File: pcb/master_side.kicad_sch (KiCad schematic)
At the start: 85 parts, among them IC1 PCA9956BTWY, J1 USB_C_Receptacle_USB2.0_14P, J2 Conn_01x02, J5 4P4C, SW1 SW_SP3T, SW10 SW_Push_45deg, SW11 SW_Push_45deg, SW12 SW_Push_45deg, SW13 SW_Push_45deg, SW14 SW_Push_45deg, SW15 SW_Push_45deg, SW16 SW_Push_45deg, SW17 SW_Push_45deg, SW18 SW_Push_45deg, SW19 SW_Push_45deg, SW2 SW_Push_45deg, SW3 SW_Push_45deg, SW4 SW_Push_45deg, SW5 SW_Push_45deg, SW6 SW_Push_45deg, SW7 SW_Push_45deg, SW8 SW_Push_45deg, SW9 SW_Push_45deg, U1 W25Q128JVSIQ, U2 RP2040, U3 NCP1117LPST33T3G, U4 OPT3001DNPR, Y1 ABM8-272-T3

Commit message: fix: revert to proper switch footprint without SMD LED
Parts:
- SW10, SW11, SW12, SW13, SW14, SW15, SW16, SW17, SW18, SW19, SW2, SW3, SW4, SW5, SW6, SW7, SW8, SW9: footprint ai03-MX_V2:MX-LED -> ai03-MX_V2:MX-Solderable-1U
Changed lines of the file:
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@@
 			)
 		)
-		(property "Footprint" "ai03-MX_V2:MX-LED"
+		(property "Footprint" "ai03-MX_V2:MX-Solderable-1U"
 			(at 384.81 298.45 0)
 			(effects
@@
 			)
 		)
-		(property "Footprint" "ai03-MX_V2:MX-LED"
+		(property "Footprint" "ai03-MX_V2:MX-Solderable-1U"
 			(at 407.67 298.45 0)
 			(effects
@@
 			)
 		)
-		(property "Footprint" "ai03-MX_V2:MX-LED"
+		(property "Footprint" "ai03-MX_V2:MX-Solderable-1U"
 			(at 396.24 326.39 0)
 			(effects
@@
 			)
 		)
-		(property "Footprint" "ai03-MX_V2:MX-LED"
+		(property "Footprint" "ai03-MX_V2:MX-Solderable-1U"
 			(at 430.53 298.45 0)
 			(effects
@@
 			)
 		)
-		(property "Footprint" "ai03-MX_V2:MX-LED"
+		(property "Footprint" "ai03-MX_V2:MX-Solderable-1U"
 			(at 384.81 326.39 0)
 			(effects
@@
 			)
 		)
-		(property "Footprint" "ai03-MX_V2:MX-LED"
+		(property "Footprint" "ai03-MX_V2:MX-Solderable-1U"
 			(at 384.81 312.42 0)
 			(effects
@@
 			)
 		)
-		(property "Footprint" "ai03-MX_V2:MX-LED"
+		(property "Footprint" "ai03-MX_V2:MX-Solderable-1U"
 			(at 407.67 312.42 0)
 			(effects
@@
 			)
 		)
-		(property "Footprint" "ai03-MX_V2:MX-LED"
+		(property "Footprint" "ai03-MX_V2:MX-Solderable-1U"
 			(at 419.1 312.42 0)
 			(effects
@@
 			)
 		)
-		(property "Footprint" "ai03-MX_V2:MX-LED"
+		(property "Footprint" "ai03-MX_V2:MX-Solderable-1U"
 			(at 373.38 312.42 0)
 			(effects
@@
 			)
 		)
-		(property "Footprint" "ai03-MX_V2:MX-LED"
+		(property "Footprint" "ai03-MX_V2:MX-Solderable-1U"
 			(at 373.38 298.45 0)
 			(effects
@@
 			)
 		)
-		(property "Footprint" "ai03-MX_V2:MX-LED"
+		(property "Footprint" "ai03-MX_V2:MX-Solderable-1U"
 			(at 430.53 326.39 0)
 			(effects
@@
 			)
 		)
-		(property "Footprint" "ai03-MX_V2:MX-LED"
+		(property "Footprint" "ai03-MX_V2:MX-Solderable-1U"
 			(at 373.38 326.39 0)
 			(effects
@@
 			)
 		)
-		(property "Footprint" "ai03-MX_V2:MX-LED"
+		(property "Footprint" "ai03-MX_V2:MX-Solderable-1U"
 			(at 430.53 312.42 0)
 			(effects
@@
 			)
 		)
-		(property "Footprint" "ai03-MX_V2:MX-LED"
+		(property "Footprint" "ai03-MX_V2:MX-Solderable-1U"
 			(at 396.24 312.42 0)
 			(effects
@@
 			)
 		)
-		(property "Footprint" "ai03-MX_V2:MX-LED"
+		(property "Footprint" "ai03-MX_V2:MX-Solderable-1U"
 			(at 407.67 326.39 0)
 			(effects
@@
 			)
 		)
-		(property "Footprint" "ai03-MX_V2:MX-LED"
+		(property "Footprint" "ai03-MX_V2:MX-Solderable-1U"
 			(at 419.1 298.45 0)
 			(effects
@@
 			)
 		)
-		(property "Footprint" "ai03-MX_V2:MX-LED"
+		(property "Footprint" "ai03-MX_V2:MX-Solderable-1U"
 			(at 396.24 298.45 0)
 			(effects
@@
 			)
 		)
-		(property "Footprint" "ai03-MX_V2:MX-LED"
+		(property "Footprint" "ai03-MX_V2:MX-Solderable-1U"
 			(at 419.1 326.39 0)
 			(effects

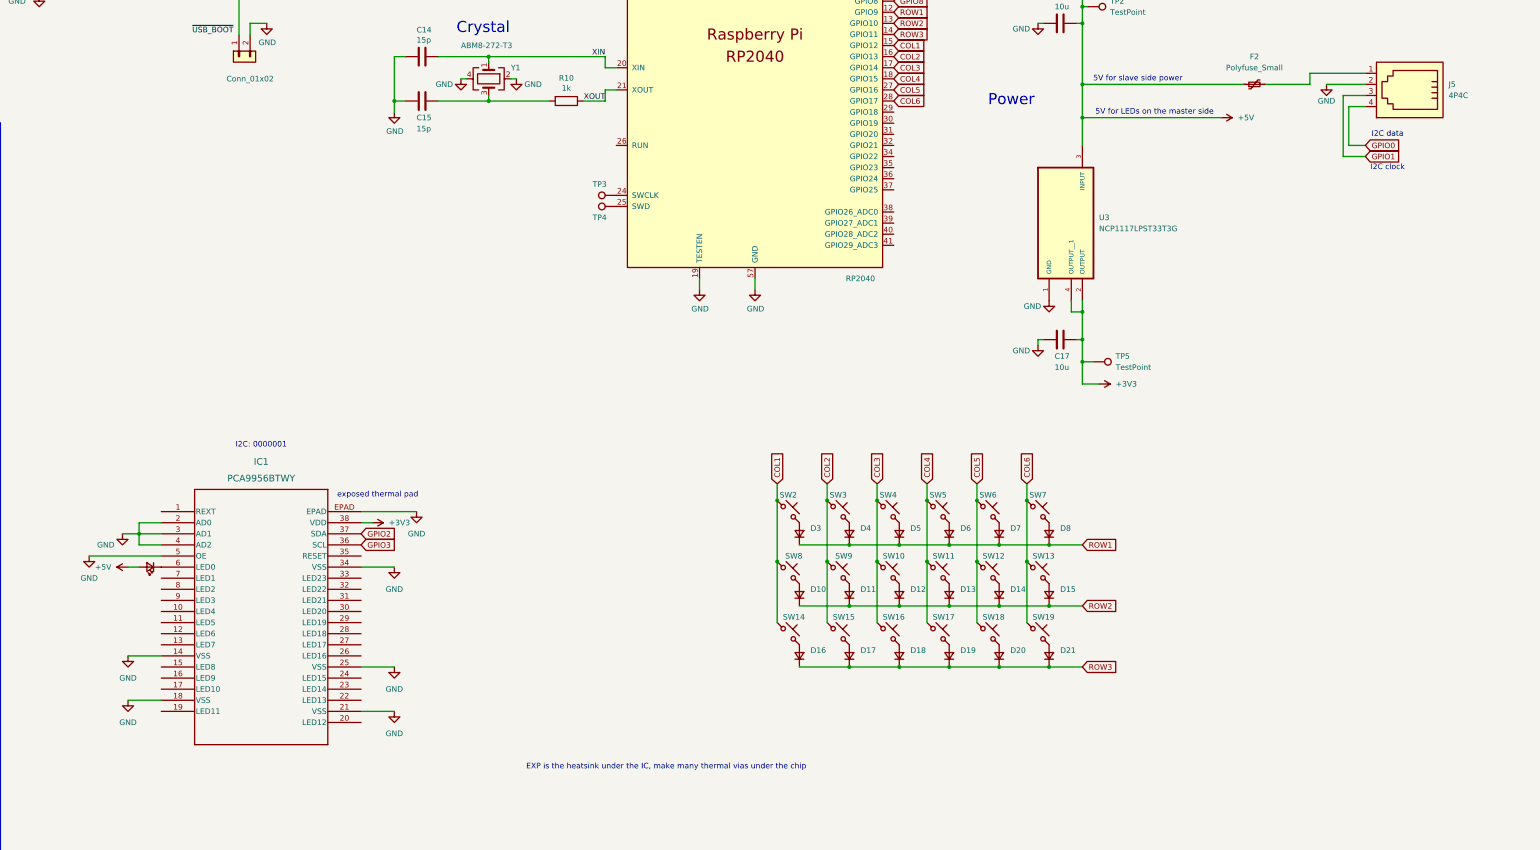
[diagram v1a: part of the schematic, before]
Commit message: fix: OE pin PCA9956B control on startup
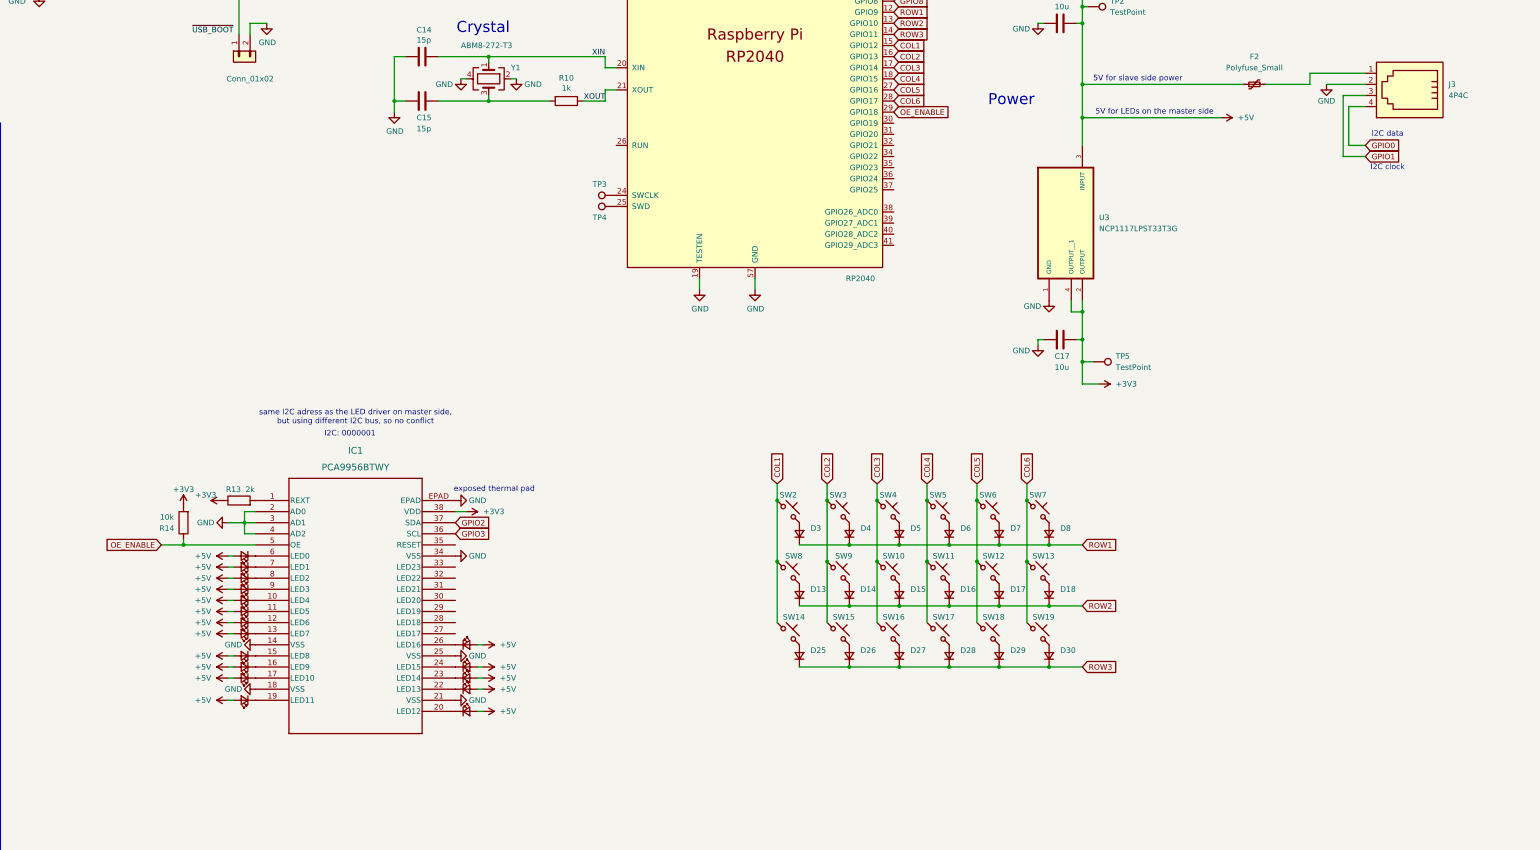
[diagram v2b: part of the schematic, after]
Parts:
- added D10, D11, D12, D19, D20, D21, D22, D23, D24, D31, D32, D33, D34, D35, D36, D37: LED_Small, LED_SMD:LED_0603_1608Metric, symbol Device:LED_Small
- added R13: 2k, Resistor_SMD:R_0402_1005Metric, symbol library:R
- added R14: 10k, Resistor_SMD:R_0402_1005Metric, symbol library:R
- D1, D2, D9: footprint (none) -> LED_SMD:LED_0603_1608Metric
- D13: renamed from D10; footprint (none) -> Diode_SMD:D_0201_0603Metric
- D14: renamed from D11; footprint (none) -> Diode_SMD:D_0201_0603Metric
- D15: renamed from D12; footprint (none) -> Diode_SMD:D_0201_0603Metric
- D16: renamed from D13; footprint (none) -> Diode_SMD:D_0201_0603Metric
- D17: renamed from D14; footprint (none) -> Diode_SMD:D_0201_0603Metric
- D18: renamed from D15; footprint (none) -> Diode_SMD:D_0201_0603Metric
- D25: renamed from D16; footprint (none) -> Diode_SMD:D_0201_0603Metric
- D26: renamed from D17; footprint (none) -> Diode_SMD:D_0201_0603Metric
- D27: renamed from D18; footprint (none) -> Diode_SMD:D_0201_0603Metric
- D28: renamed from D19; footprint (none) -> Diode_SMD:D_0201_0603Metric
- D29: renamed from D20; footprint (none) -> Diode_SMD:D_0201_0603Metric
- D3, D4, D5, D6, D7, D8: footprint (none) -> Diode_SMD:D_0201_0603Metric
- D30: renamed from D21; footprint (none) -> Diode_SMD:D_0201_0603Metric
- R3, R4, R5, R6: footprint (none) -> Resistor_SMD:R_0402_1005Metric
- SW1: footprint (none) -> Button_Switch_SMD:SW_SP3T_PCM13
- renumbered J5 to J3
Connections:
- net +3V3: now also R13.1, R14.2
- net +5V: now also D10.2 (A), D11.2 (A), D12.2 (A), D19.2 (A), D20.2 (A), D21.2 (A), D22.2 (A), D23.2 (A), D24.2 (A), D31.2 (A), D32.2 (A), D33.2 (A), D34.2 (A), D35.2 (A), D36.2 (A), D37.2 (A)
- net GND: no longer IC1.5 (OE)
- net OE_ENABLE: now reaches U2.29 (GPIO18)
- net OE_ENABLE: now also IC1.5 (OE), R14.1
- net at IC1.1 (REXT): now also R13.2
- net at IC1.10 (LED4): now also D19.1 (K)
- net at IC1.11 (LED5): now also D20.1 (K)
- net at IC1.12 (LED6): now also D21.1 (K)
- net at IC1.13 (LED7): now also D22.1 (K)
- net at IC1.15 (LED8): now also D24.1 (K)
- net at IC1.16 (LED9): now also D31.1 (K)
- net at IC1.17 (LED10): now also D33.1 (K)
- net at IC1.19 (LED11): now also D36.1 (K)
- net at IC1.20 (LED12): now also D37.1 (K)
- net at IC1.22 (LED13): now also D35.1 (K)
- net at IC1.23 (LED14): now also D34.1 (K)
- net at IC1.24 (LED15): now also D32.1 (K)
- net at IC1.26 (LED16): now also D23.1 (K)
- net at IC1.7 (LED1): now also D10.1 (K)
- net at IC1.8 (LED2): now also D11.1 (K)
- net at IC1.9 (LED3): now also D12.1 (K)
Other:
- note added: "same I2C adress as the LED driver on master side, but using different I2C bus, so no conflict"
- note removed: "EXP is the heatsink under the IC, make many thermal vias under the chip"

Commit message: fix: PCA9956 OE pin and RESET pin and improve LED power delivery
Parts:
- removed J2: Conn_01x02, Connector_PinHeader_2.54mm:PinHeader_1x02_P2.54mm_Vertical, symbol library:Conn_01x02
- added C18: 10u, symbol Device:C
- added R14: 10k, Resistor_SMD:R_0402_1005Metric, symbol library:R
- added SW1: SW_Push, Button_Switch_SMD:SW_SPST_TL3342, symbol Switch:SW_Push
- F1, F2: footprint (none) -> Fuse:Fuse_1206_3216Metric
- renumbered J3 to J2, R14 to R15, SW9 to SW10, SW10 to SW11, SW11 to SW12, SW12 to SW13, SW13 to SW14, SW14 to SW15, SW15 to SW16, SW16 to SW17, SW17 to SW18, SW18 to SW19, SW1 to SW2, SW19 to SW20, SW2 to SW3, SW3 to SW4, SW4 to SW5, SW5 to SW6, SW6 to SW7, SW7 to SW8, SW8 to SW9
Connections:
- net +3V3: now also R14.1; no longer R13.1
- net +5V: now also C18.1
- net GND: now also R13.1, C18.2, SW1.1
- net at R9.2: now also SW1.2
- net at IC1.35 (RESET): now also R14.2
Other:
- note added: "RP2040 persents itself as a USB storage device when this is pressed"

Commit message: fix: Diode & switch numbering for kbplacer
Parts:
- added C17: 100n, Capacitor_SMD:C_0805_2012Metric, symbol Device:C
- added LD9: LED_Small, LED_SMD:LED_0603_1608Metric, symbol Device:LED_Small
- added R11: 10k, Resistor_SMD:R_0402_1005Metric, symbol library:R
- added SW20: SW_Push, Button_Switch_SMD:SW_SPST_TL3342, symbol Switch:SW_Push
- C19: renamed from C18; footprint (none) -> Capacitor_SMD:C_0805_2012Metric
- R1, R2: value 27,4 -> 27
- renumbered C17 to C16, C16 to C18, D3 to D1, D16 to D10, D17 to D11, D18 to D12, D25 to D13, D26 to D14, D27 to D15, D28 to D16, D29 to D17, D30 to D18, D1 to D19, D4 to D2, D2 to D20, D5 to D3, D6 to D4, D7 to D5, D8 to D6, D13 to D7, D14 to D8, D15 to D9, D9 to LD1, D23 to LD10, D24 to LD11, D31 to LD12, D32 to LD13, D33 to LD14, D34 to LD15, D35 to LD16, D36 to LD17, D37 to LD18, D10 to LD2, D11 to LD3, D12 to LD4, D19 to LD5, D20 to LD6, D21 to LD7, D22 to LD8, R13 to R12, R11 to R13, R15 to R14, R14 to R15, R12 to R16, SW3 to SW1, SW12 to SW10, SW13 to SW11, SW14 to SW12, SW15 to SW13, SW16 to SW14, SW17 to SW15, SW18 to SW16, SW19 to SW17, SW20 to SW18, SW1 to SW19, SW4 to SW2, SW2 to SW21, SW5 to SW3, SW6 to SW4, SW7 to SW5, SW8 to SW6, SW9 to SW7, SW10 to SW8, SW11 to SW9
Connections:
- net +3V3: now also C17.1, R11.1
- net +5V: now also LD9.2 (A)
- net GND: now also C17.2, SW20.1
- net at U2.26 (RUN): now also R11.2, SW20.2
- net at IC1.27 (LED17): now also LD9.1 (K)
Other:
- note added: "Make sure C11 is close to pin 45 of RP2040"
- note added: "backlight LED driver"
- note added: "light sensor"
- note removed: "Make sure C8 is close to pin 45 of RP2040"
- note removed: "exposed thermal pad"
- moved on the sheet: C1, C10, C11, C12, C13, C14, C15, C16, C18, C19, C2, C3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

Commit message: feat: Better global label names
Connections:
- net GPIO0 renamed I2C_D_R
- net GPIO1 renamed I2C_CLK_R
- net GPIO2 renamed I2C_D
- net GPIO3 renamed I2C_CLK
- net GPIO4 renamed STATUS1
- net GPIO5 renamed STATUS2
- net GPIO6 renamed BL_DIM_1
- net GPIO7 renamed BL_DIM_2
- net GPIO8 renamed BL_DIM_3
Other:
- note added: "Enable internal pull-ups on GPIO6, 7 and 8"
- note removed: "Enable internal pull-up on GPIO6, 7 and 8"
- moved on the sheet: C1, C10, C11, C12, C13, C14, C15, C16, C17, C18, C19, C2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

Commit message: fix: Proper USB-C receptacle symbol
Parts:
- removed J1: USB_C_Receptacle_USB2.0_14P, Connector_USB:USB_C_Receptacle_GCT_USB4085, symbol Connector:USB_C_Receptacle_USB2.0_14P
- added J4: USB_C_Receptacle_USB2.0_16P, Connector_USB:USB_C_Receptacle_GCT_USB4105-xx-A_16P_TopMnt_Horizontal, symbol Connector:USB_C_Receptacle_USB2.0_16P
- renumbered SW19 to OSW1, SW20 to OSW2, SW21 to OSW3, R14 to R13, R15 to R14, R13 to R15
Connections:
- net GND: now also J4.A1 (GND), J4.A12 (GND), J4.B1 (GND), J4.B12 (GND), J4.S1 (SHIELD)
- net USB_D+: now also J4.A6 (D+), J4.B6 (D+)
- net USB_D-: now also J4.A7 (D-), J4.B7 (D-)
- net at F1.1: now also J4.A4 (VBUS), J4.A9 (VBUS), J4.B4 (VBUS), J4.B9 (VBUS)
- net at R7.2: now also J4.B5 (CC2)
- net at R8.2: now also J4.A5 (CC1)
